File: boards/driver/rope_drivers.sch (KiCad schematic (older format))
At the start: 0 parts

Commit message: Driver board: finished first rough draft schematic. Lots of placeholders, but at least every place is held.
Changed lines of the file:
@@
 $Descr USLedger 17000 11000
 encoding utf-8
-Sheet 31 68
+Sheet 31 69
 Title ""
 Date ""
@@
 	6200 1300 9000 1300
 Text Label 10950 7800 2    50   ~ 0
-XCN08
+XCN8
 Wire Wire Line
 	10650 7800 10950 7800
@@
 	9900 8050 9550 8050
 Text Label 9650 7800 0    50   ~ 0
-~IL08
+~IL8
 Wire Wire Line
 	9900 7800 9650 7800
@@
 	8900 5850 9900 5850
 Text Label 10950 7100 2    50   ~ 0
-XCN07
+XCN7
 Wire Wire Line
 	10650 7100 10950 7100
@@
 	9900 7350 9550 7350
 Text Label 9650 7100 0    50   ~ 0
-~IL07
+~IL7
 Wire Wire Line
 	9900 7100 9650 7100
@@
 $EndSheet
 Text Label 10950 6400 2    50   ~ 0
-XCN06
+XCN6
 Wire Wire Line
 	10650 6400 10950 6400
 Text Label 9650 6400 0    50   ~ 0
-~IL06
+~IL6
 Wire Wire Line
 	9900 6400 9650 6400
@@
 	9900 6650 9550 6650
 Text Label 10950 5700 2    50   ~ 0
-XCN05
+XCN5
 Wire Wire Line
 	10650 5700 10950 5700
@@
 	9900 5950 9550 5950
 Text Label 9650 5700 0    50   ~ 0
-~IL05
+~IL5
 Wire Wire Line
 	9900 5700 9650 5700
@@
 $EndSheet
 Text Label 10950 4950 2    50   ~ 0
-XCN04
+XCN4
 Wire Wire Line
 	10650 4950 10950 4950
 Text Label 9650 4950 0    50   ~ 0
-~IL04
+~IL4
 Wire Wire Line
 	9900 4950 9650 4950
@@
 	9900 5200 9550 5200
 Text Label 10950 4250 2    50   ~ 0
-XCN03
+XCN3
 Wire Wire Line
 	10650 4250 10950 4250
@@
 	9000 4400 9900 4400
 Text Label 9650 4250 0    50   ~ 0
-~IL03
+~IL3
 Wire Wire Line
 	9900 4250 9650 4250
@@
 	9000 3700 9900 3700
 Text Label 10950 3550 2    50   ~ 0
-XCN02
+XCN2
 Wire Wire Line
 	10650 3550 10950 3550
 Text Label 9650 3550 0    50   ~ 0
-~IL02
+~IL2
 Wire Wire Line
 	9900 3550 9650 3550
@@
 	9900 3800 9550 3800
 Text Label 10950 2850 2    50   ~ 0
-XCN01
+XCN1
 Wire Wire Line
 	10650 2850 10950 2850
@@
 	9000 3000 9900 3000
 Text Label 9650 2850 0    50   ~ 0
-~IL01
+~IL1
 Wire Wire Line
 	9900 2850 9650 2850
@@
 	6200 7950 7100 7950
 Text Label 8150 7800 2    50   ~ 0
-XFN08
+XFN8
 Wire Wire Line
 	7850 7800 8150 7800
@@
 	7100 8050 6750 8050
 Text Label 6850 7800 0    50   ~ 0
-IL08
+IL8
 Wire Wire Line
 	7100 7800 6850 7800
@@
 	6200 3700 6200 4400
 Text Label 8150 7100 2    50   ~ 0
-XFN07
+XFN7
 Wire Wire Line
 	7850 7100 8150 7100
@@
 	7100 7350 6750 7350
 Text Label 6850 7100 0    50   ~ 0
-IL07
+IL7
 Wire Wire Line
 	7100 7100 6850 7100
@@
 $EndSheet
 Text Label 8150 6400 2    50   ~ 0
-XFN06
+XFN6
 Wire Wire Line
 	7850 6400 8150 6400
 Text Label 6850 6400 0    50   ~ 0
-IL06
+IL6
 Wire Wire Line
 	7100 6400 6850 6400
@@
 	7100 6650 6750 6650
 Text Label 8150 5700 2    50   ~ 0
-XFN05
+XFN5
 Wire Wire Line
 	7850 5700 8150 5700
@@
 	7100 5950 6750 5950
 Text Label 6850 5700 0    50   ~ 0
-IL05
+IL5
 Wire Wire Line
 	7100 5700 6850 5700
@@
 	6200 5100 7100 5100
 Text Label 8150 4950 2    50   ~ 0
-XFN04
+XFN4
 Wire Wire Line
 	7850 4950 8150 4950
 Text Label 6850 4950 0    50   ~ 0
-IL04
+IL4
 Wire Wire Line
 	7100 4950 6850 4950
@@
 	7100 5200 6750 5200
 Text Label 8150 4250 2    50   ~ 0
-XFN03
+XFN3
 Wire Wire Line
 	7850 4250 8150 4250
@@
 	6200 4400 7100 4400
 Text Label 6850 4250 0    50   ~ 0
-IL03
+IL3
 Wire Wire Line
 	7100 4250 6850 4250
@@
 	6200 3000 6200 3700
 Text Label 8150 3550 2    50   ~ 0
-XFN02
+XFN2
 Wire Wire Line
 	7850 3550 8150 3550
 Text Label 6850 3550 0    50   ~ 0
-IL02
+IL2
 Wire Wire Line
 	7100 3550 6850 3550
@@
 	7100 3800 6750 3800
 Text Label 8150 2850 2    50   ~ 0
-XFN01
+XFN1
 Wire Wire Line
 	7850 2850 8150 2850
@@
 	6200 3000 7100 3000
 Text Label 6850 2850 0    50   ~ 0
-IL01
+IL1
 Wire Wire Line
 	7100 2850 6850 2850
@@
 	14500 3700 14800 3700
 Text Label 14800 3700 2    50   ~ 0
-RFD01
+RFD1
 Wire Wire Line
 	14500 3800 14800 3800
 Text Label 14800 3800 2    50   ~ 0
-RFD02
+RFD2
 Wire Wire Line
 	14500 3900 14800 3900
 Text Label 14800 3900 2    50   ~ 0
-RFD03
+RFD3
 Wire Wire Line
 	14500 4000 14800 4000
 Text Label 14800 4000 2    50   ~ 0
-RFD04
+RFD4
 Wire Wire Line
 	14500 4150 14950 4150
 Text Label 14800 4150 2    50   ~ 0
-RCD01
+RCD1
 Wire Wire Line
 	14500 4250 14950 4250
 Text Label 14800 4250 2    50   ~ 0
-RCD02
+RCD2
 Wire Wire Line
 	14500 4350 14950 4350
 Text Label 14800 4350 2    50   ~ 0
-RCD03
+RCD3
 Wire Wire Line
 	14500 4450 14950 4450
 Text Label 14800 4450 2    50   ~ 0
-RCD04
+RCD4
 Wire Wire Line
 	14500 4600 15100 4600
@@
 	14500 5300 14800 5300
 Text Label 14800 5300 2    50   ~ 0
-RFD05
+RFD5
 Wire Wire Line
 	14500 5400 14800 5400
 Text Label 14800 5400 2    50   ~ 0
-RFD06
+RFD6
 Wire Wire Line
 	14500 5500 14800 5500
 Text Label 14800 5500 2    50   ~ 0
-RFD07
+RFD7
 Wire Wire Line
 	14500 5600 14800 5600
 Text Label 14800 5600 2    50   ~ 0
-RFD08
+RFD8
 Wire Wire Line
 	14500 5750 14950 5750
 Text Label 14800 5750 2    50   ~ 0
-RCD05
+RCD5
 Wire Wire Line
 	14500 5850 14950 5850
-Text Label 14800 5850 2    50   ~ 0
-RCD06
 Wire Wire Line
 	14500 5950 14950 5950
-Text Label 14800 5950 2    50   ~ 0
-RCD07
 Wire Wire Line
 	14500 6050 14950 6050
 Text Label 14800 6050 2    50   ~ 0
-RCD08
+RCD8
 Wire Wire Line
 	14500 6200 15100 6200
@@
 Connection ~ 6200 1300
 Text HLabel 6700 2700 0    50   Input ~ 0
-IL[01..08]
+IL[1..8]
 Entry Wire Line
 	9550 2750 9650 2850
@@
 	9550 2700 9500 2700
 Text HLabel 9500 2700 0    50   Input ~ 0
-~IL[01..08]
+~IL[1..8]
 Entry Wire Line
 	8150 2850 8250 2750
@@
 	8250 2700 8300 2700
 Text HLabel 8300 2700 2    50   Output ~ 0
-XFN[01..08]
+XFN[1..8]
 Entry Wire Line
 	10950 2850 11050 2750
@@
 	11050 2700 11100 2700
 Text HLabel 11100 2700 2    50   Output ~ 0
-XCN[01..08]
+XCN[1..8]
 Entry Wire Line
 	14800 3700 14900 3600
@@
 	14900 3550 15400 3550
 Text HLabel 15400 3550 2    50   Output ~ 0
-RFD[01..08]
+RFD[1..8]
 Entry Wire Line
 	14950 4150 15050 4050
@@
 	15050 4000 15400 4000
 Text HLabel 15400 4000 2    50   Output ~ 0
-RCD[01..08]
+RCD[1..8]
 Entry Wire Line
 	15100 4600 15200 4500
@@
 Text Notes 2300 900  2    50   ~ 0
 Filtered Power
+Text Label 14800 5950 2    50   ~ 0
+RCD7
+Text Label 14800 5850 2    50   ~ 0
+RCD6
 Wire Bus Line
 	1750 3850 1750 4600

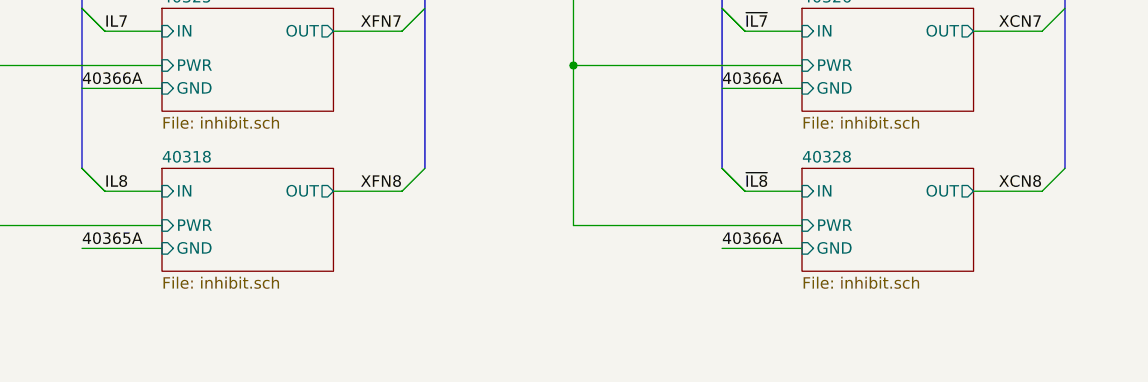
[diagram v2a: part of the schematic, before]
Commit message: Driver board: integrated DIN 41612 backplane connector, and made a dedicated parity inhibit sheet with a different set resistor value.
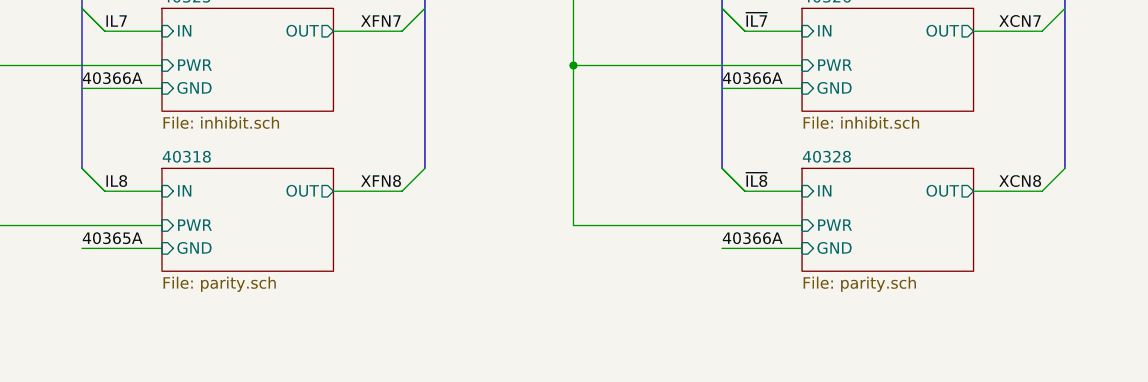
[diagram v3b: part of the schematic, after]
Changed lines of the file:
@@
 Wire Wire Line
 	9900 7800 9650 7800
-$Sheet
-S 9900 7700 750  450
-U 624B82F7
-F0 "40328" 50
-F1 "inhibit.sch" 50
-F2 "IN" I L 9900 7800 50
-F3 "PWR" I L 9900 7950 50
-F4 "OUT" O R 10650 7800 50
-F5 "GND" I L 9900 8050 50
-$EndSheet
 Wire Wire Line
 	8900 7250 9900 7250
@@
 Wire Wire Line
 	7100 7800 6850 7800
-$Sheet
-S 7100 7700 750  450
-U 62495C8E
-F0 "40318" 50
-F1 "inhibit.sch" 50
-F2 "IN" I L 7100 7800 50
-F3 "PWR" I L 7100 7950 50
-F4 "OUT" O R 7850 7800 50
-F5 "GND" I L 7100 8050 50
-$EndSheet
 Connection ~ 6100 6550
 Wire Wire Line
@@
 Text Label 14800 5850 2    50   ~ 0
 RCD6
+$Sheet
+S 7100 7700 750  450
+U 61A931FB
+F0 "40318" 50
+F1 "parity.sch" 50
+F2 "IN" I L 7100 7800 50
+F3 "PWR" I L 7100 7950 50
+F4 "OUT" O R 7850 7800 50
+F5 "GND" I L 7100 8050 50
+$EndSheet
+$Sheet
+S 9900 7700 750  450
+U 61AB4CBE
+F0 "40328" 50
+F1 "parity.sch" 50
+F2 "IN" I L 9900 7800 50
+F3 "PWR" I L 9900 7950 50
+F4 "OUT" O R 10650 7800 50
+F5 "GND" I L 9900 8050 50
+$EndSheet
 Wire Bus Line
 	1750 3850 1750 4600
